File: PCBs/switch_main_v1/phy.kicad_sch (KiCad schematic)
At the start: 1 part, among them U501 DP83867CSRGZR

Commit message: Schematic progress
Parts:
- added C501, C502, C506, C507, C508, C519, C520, C525, C526, C527, C532: 100n, Capacitor_SMD:C_0402_1005Metric, symbol Device:C_Small
- added C503, C504, C505: 27p, Capacitor_SMD:C_0402_1005Metric, symbol Device:C_Small
- added C509, C510, C511, C512, C513, C521, C522, C528, C529, C530, C533: 1u, Capacitor_SMD:C_0402_1005Metric, symbol Device:C_Small
- added C514, C516, C518, C524: 10n, Capacitor_SMD:C_0402_1005Metric, symbol Device:C_Small
- added C515, C517, C523, C531: 10u, Capacitor_SMD:C_0402_1005Metric, symbol Device:C_Small
- added R501: 11k, Resistor_SMD:R_0402_1005Metric, symbol Device:R_Small
- added Y501: ECS-250-18-36B2-CTY-TR, Crystal:Crystal_SMD_2520-4Pin_2.5x2.0mm, symbol Device:Crystal_GND24_Small
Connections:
- net ETHERNET.TD0_P: now reaches U501.1 (TD_P_A)
- net ETHERNET.TD3_P: now reaches U501.10 (TD_P_D)
- net ETHERNET.TD3_N: now reaches U501.11 (TD_M_D)
- net RBIAS: now reaches U501.12 (RBIAS)
- net RBIAS: now also R501.1
- net +1V8: now reaches U501.13 (VDDA1P8_1)
- net +1V8: now also U501.48 (VDDA1P8_2), C518.2, C519.2, C520.2, C521.2, C522.2, C523.2
- net XO: now reaches U501.14 (XO)
- net XO: now also C505.1, Y501.1
- net XI: now reaches U501.15 (XI)
- net XI: now also C503.1, C504.1, Y501.3
- net SMI.MDIO: now reaches U501.16 (MDC)
- net SMI.MDC: now reaches U501.17 (MDIO)
- net CLK_OUT: now reaches U501.18 (CLK_OUT)
- net +2V5: now reaches U501.19 (VDDIO_1)
- net +2V5: now also U501.3 (VDDA2P5_1), U501.30 (VDDIO_2), U501.41 (VDDIO_3), U501.9 (VDDA2P5_2), C501.2, C502.2, C506.2, C507.2, C508.2, C509.2, C510.2, C511.2, C512.2, C513.2, C514.2, C515.2, C516.2, C517.2
- net ETHERNET.TD0_N: now reaches U501.2 (TD_M_A)
- net +1V0: now reaches U501.24 (VDD1P0_2)
- net +1V0: now also U501.31 (VDD1P0_3), U501.42 (VDD1P0_4), U501.6 (VDD1P0_1), C524.2, C525.2, C526.2, C527.2, C528.2, C529.2, C530.2, C531.2, C532.2, C533.2
- net RGMII.TX_D3: now reaches U501.25 (TX_D3)
- net RGMII.TX_D2: now reaches U501.26 (TX_D2)
- net RGMII.TX_D1: now reaches U501.27 (TX_D1/SGMII_SIP)
- net RGMII.TX_D0: now reaches U501.28 (TX_D0/SGMII_SIN)
- net RGMII.TX_CLK: now reaches U501.29 (GTX_CLK)
- net RGMII.RX_CLK: now reaches U501.32 (RX_CLK)
- net RGMII.RX_D0: now reaches U501.33 (RX_D0/SGMII_COP)
- net RGMII.RX_D1: now reaches U501.34 (RX_D1/SGMII_CON)
- net RGMII.RX_D2: now reaches U501.35 (RX_D2/SGMII_SOP)
- net RGMII.RX_D3: now reaches U501.36 (RX_D3/SGMII_SON)
- net RGMII.TX_CTRL: now reaches U501.37 (TX_CTRL)
- net RGMII.RX_CTRL: now reaches U501.38 (RX_CTRL)
- net ETHERNET.TD1_P: now reaches U501.4 (TD_P_B)
- net GND: now reaches U501.49 (GND)
- net GND: now also C501.1, C502.1, C504.2, C505.2, C506.1, C507.1, C508.1, C509.1, C510.1, C511.1, C512.1, C513.1, C514.1, C515.1, C516.1, C517.1, C518.1, C519.1, C520.1, C521.1, C522.1, C523.1, C524.1, C525.1, C526.1, C527.1, C528.1, C529.1, C530.1, C531.1, C532.1, C533.1, R501.2, Y501.2, Y501.4
- net ETHERNET.TD1_N: now reaches U501.5 (TD_M_B)
- net ETHERNET.TD2_P: now reaches U501.7 (TD_P_C)
- net ETHERNET.TD2_N: now reaches U501.8 (TD_M_C)
- new net CLK_IN: C503.2
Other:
- note added: "VDD1P0"
- note added: "VDDA1P8"
- note added: "VDDA2P5"
- note added: "VDDIO"
- note removed: "ESD PROTECTION"
- moved on the sheet: U501

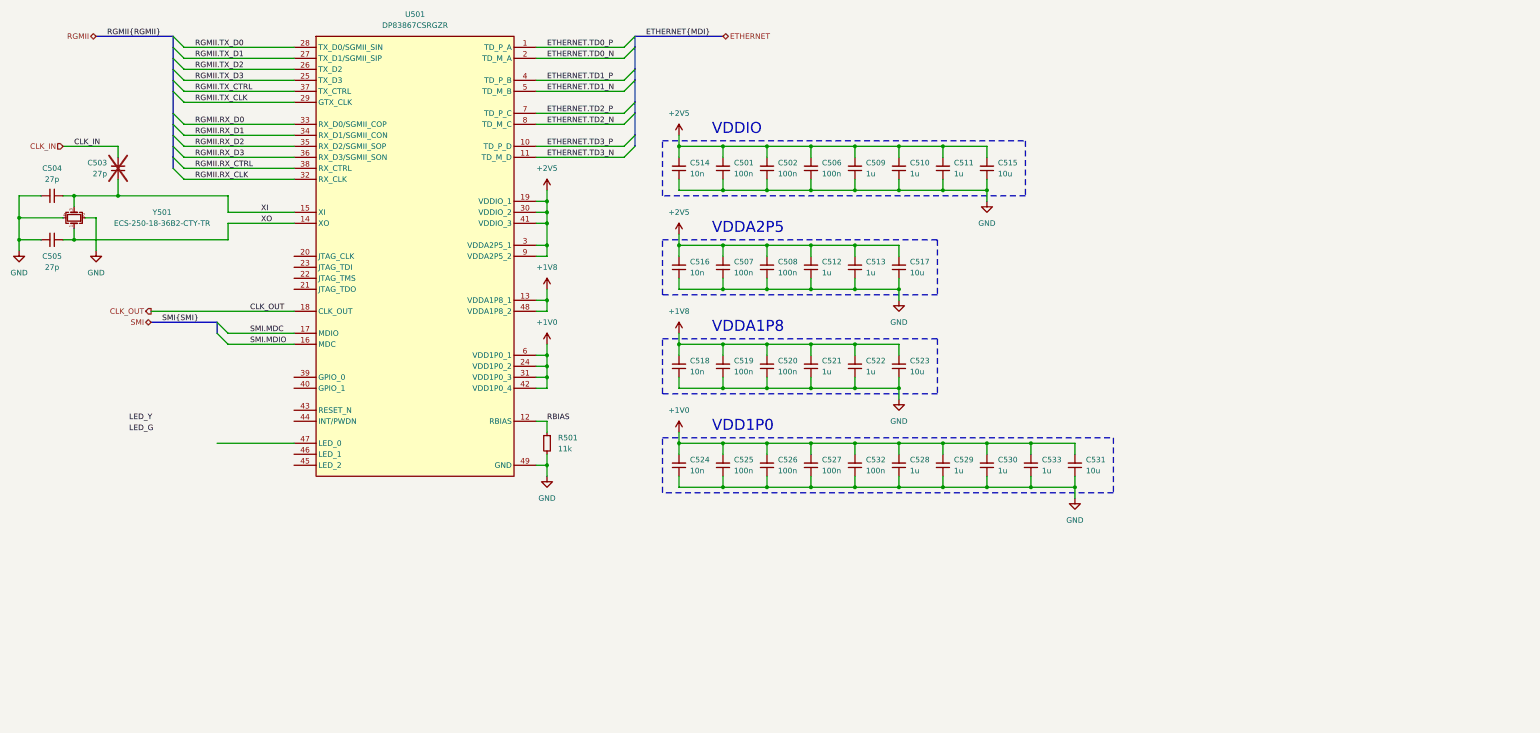
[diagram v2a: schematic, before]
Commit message: GbE part of schematic done
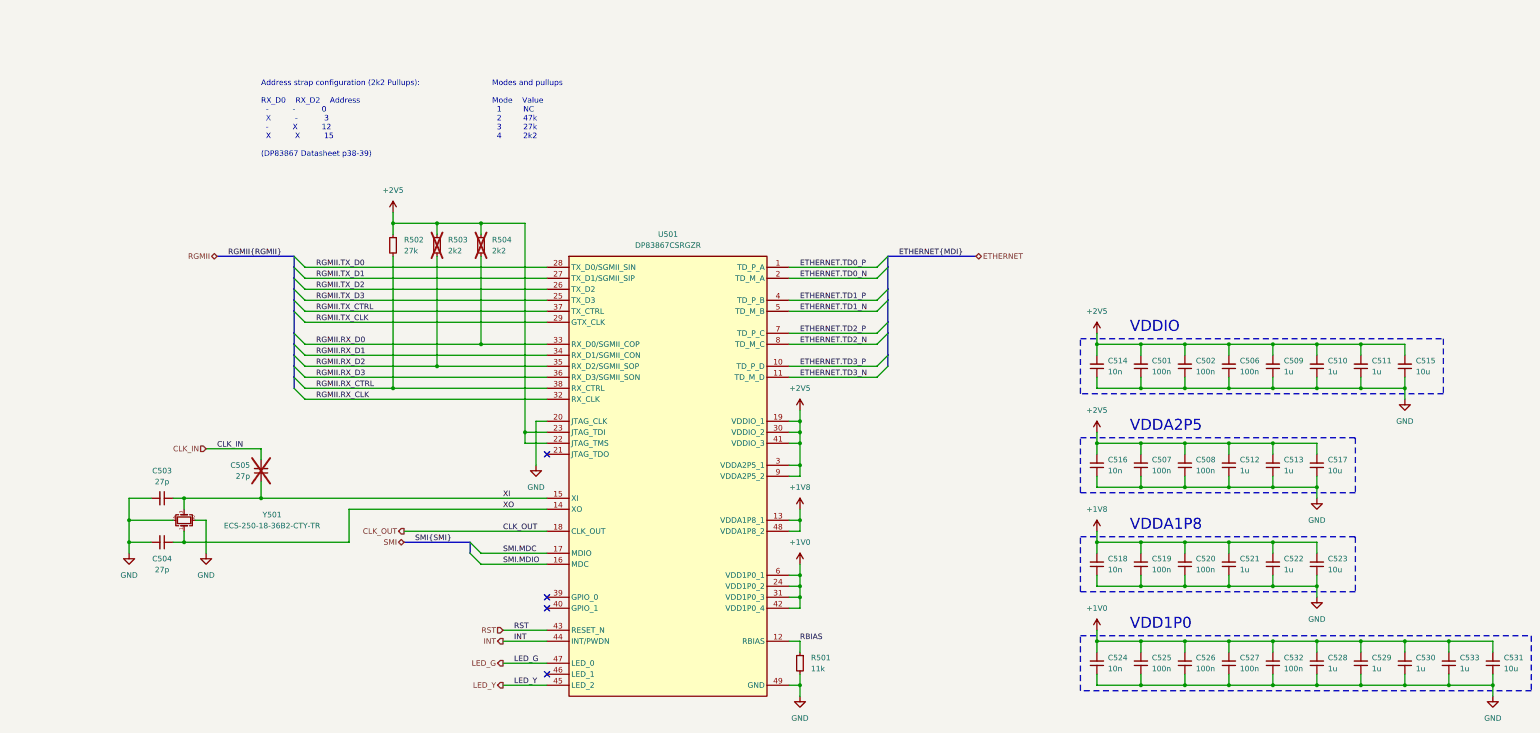
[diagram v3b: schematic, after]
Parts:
- added R502: 27k, Resistor_SMD:R_0402_1005Metric, symbol Device:R_Small
- added R503, R504: 2k2, Resistor_SMD:R_0402_1005Metric, symbol Device:R_Small
- C503: now fitted; now in the parts list
- C505: now not fitted; now left out of the parts list
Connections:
- net +2V5: now also U501.22 (JTAG_TMS), U501.23 (JTAG_TDI), R502.1, R503.1, R504.1
- net CLK_IN: now also C505.2; no longer C503.2
- net GND: now also C503.2, U501.20 (JTAG_CLK); no longer C505.2
- net LED_G: now also U501.47 (LED_0)
- net LED_Y: now also U501.45 (LED_2)
- net RGMII.RX_CTRL: now also R502.2
- net RGMII.RX_D0: now also R504.2
- net RGMII.RX_D2: now also R503.2
- net XI: now also C505.1; no longer C504.1
- net XO: now also C504.1; no longer C505.1
- net RST: now reaches U501.43 (RESET_N)
- net INT: now reaches U501.44 (INT/PWDN)
- no-connect marks 0 -> 4
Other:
- note added: "Address strap configuration (2k2 Pullups): RX_D0 RX_D2 Address - - 0 X - 3 - X 12 X X 15 (DP83867 Datasheet p38-39)"
- note added: "Modes and pullups Mode Value 1 NC 2 47k 3 27k 4 2k2"
- company: (none) -> Ben Smith
- moved on the sheet: C501, C502, C506, C507, C508, C509, C510, C511, C512, C513, C514, C515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

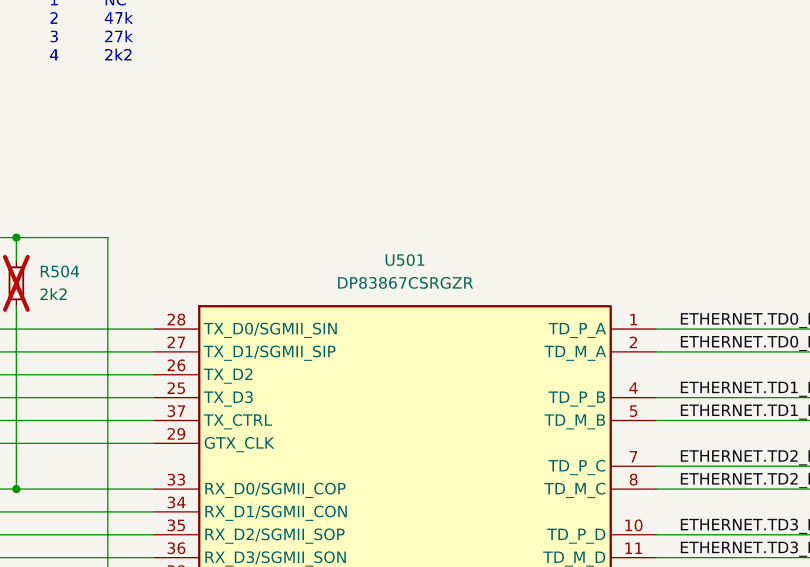
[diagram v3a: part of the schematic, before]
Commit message: Changed MCU to STM32H573VIT3Q
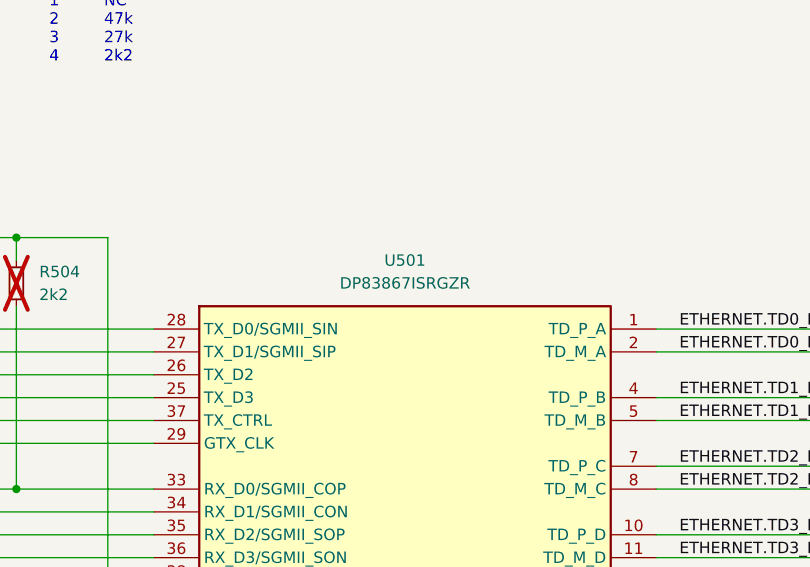
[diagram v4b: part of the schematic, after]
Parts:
- U501: value DP83867CSRGZR -> DP83867ISRGZR
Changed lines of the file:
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@@
 			)
 		)
-		(property "Datasheet" "~"
+		(property "Datasheet" "https://www.mouser.co.uk/datasheet/2/122/ECX_2236B2-2400583.pdf"
 			(at 66.04 160.02 0)
 			(effects
@@
 			)
 		)
-		(property "Value" "DP83867CSRGZR"
+		(property "Value" "DP83867ISRGZR"
 			(at 177.8 96.52 0)
 			(effects
